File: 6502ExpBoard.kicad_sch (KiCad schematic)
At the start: 40 parts, among them J2 Expansion / Diag Port, U1 74LS373, U2 74LS373, U4 74LS373

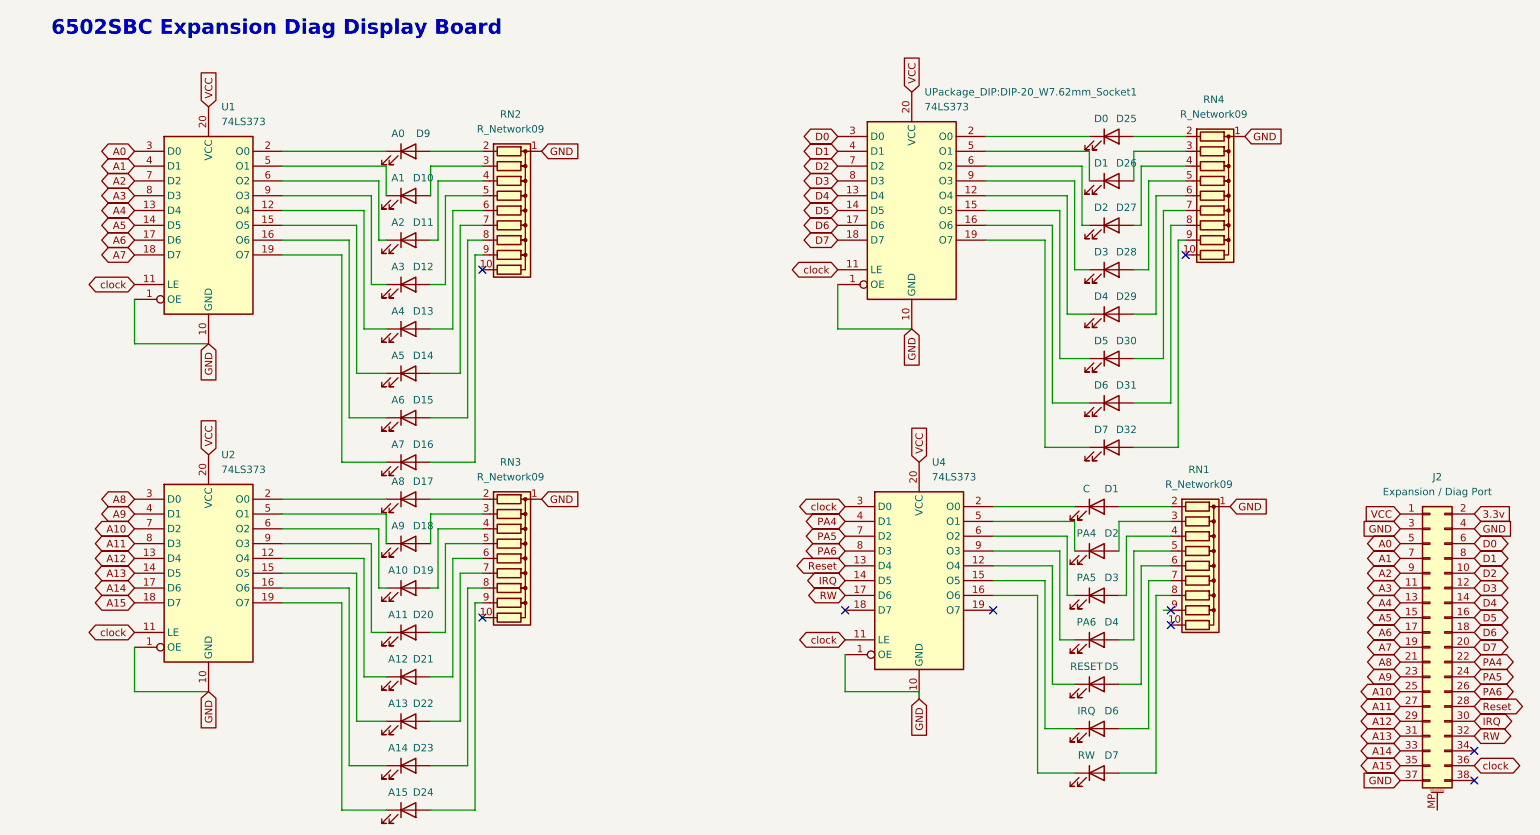
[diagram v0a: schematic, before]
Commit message: Diag Board led fixes
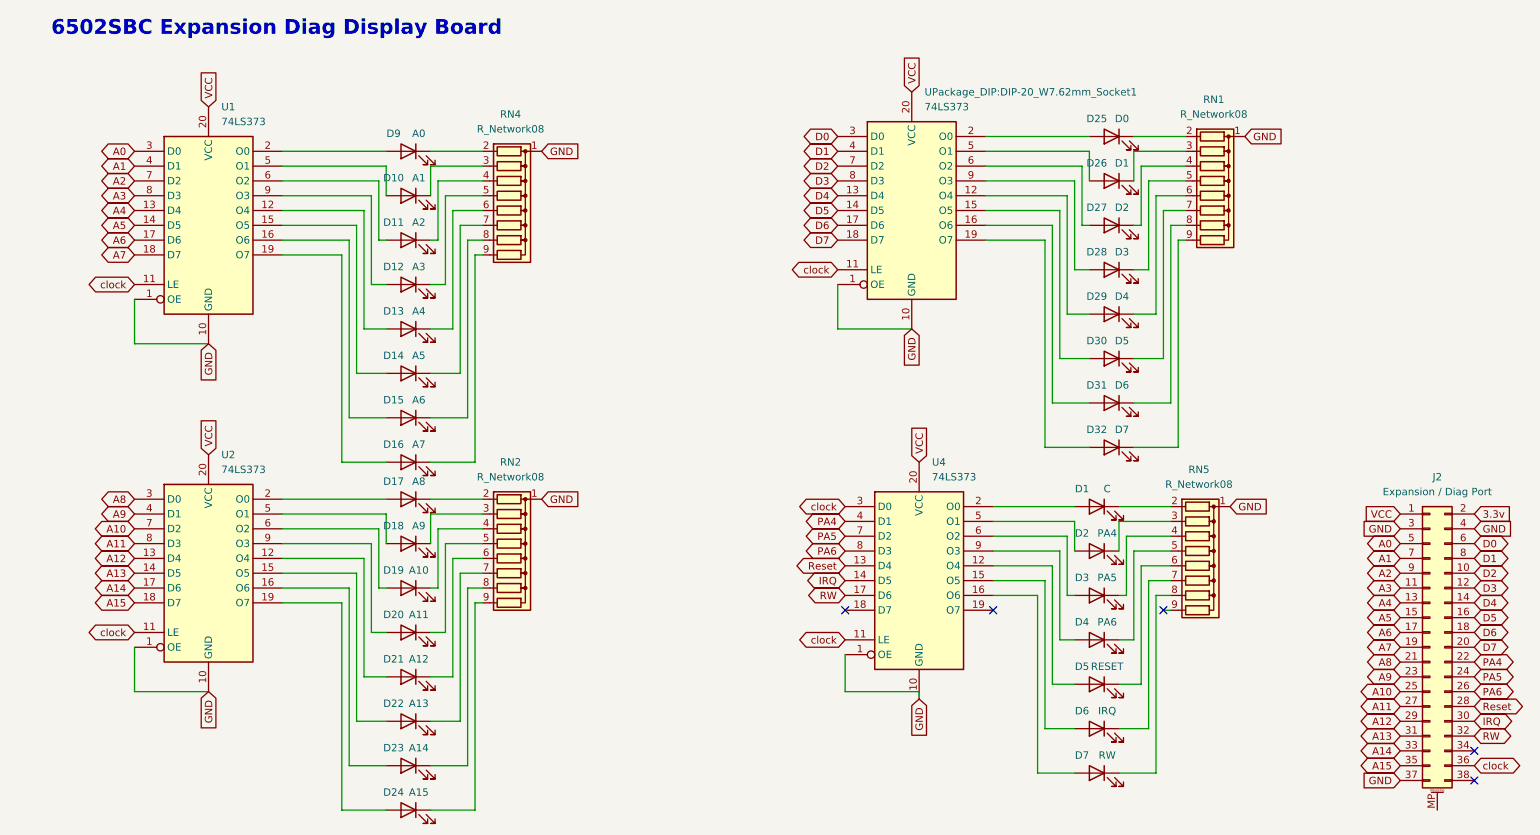
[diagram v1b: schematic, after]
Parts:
- removed RN1, RN2, RN3, RN4: R_Network09, Resistor_THT:R_Array_SIP10, symbol Device:R_Network09
- added RN1, RN2, RN4, RN5: R_Network08, Resistor_THT:R_Array_SIP9, symbol Device:R_Network08
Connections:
- net GND: now also RN1.1 (common), RN2.1 (common), RN4.1 (common), RN5.1 (common)
- net at D18.1 (K): now also RN2.3 (R2); no longer U2.5 (O1)
- net at D18.2 (A): now also U2.5 (O1)
- net at D24.1 (K): now also RN2.9 (R8); no longer U2.19 (O7)
- net at D24.2 (A): now also U2.19 (O7)
- net at D6.1 (K): now also RN5.7 (R6); no longer U4.15 (O5)
- net at D6.2 (A): now also U4.15 (O5)
- net at U4.12 (O4): now also D5.2 (A); no longer D5.1 (K)
- net at U4.16 (O6): now also D7.2 (A); no longer D7.1 (K)
- net at U4.2 (O0): now also D1.2 (A); no longer D1.1 (K)
- net at U4.5 (O1): now also D2.2 (A); no longer D2.1 (K)
- net at U4.6 (O2): now also D3.2 (A); no longer D3.1 (K)
- net at U4.9 (O3): now also D4.2 (A); no longer D4.1 (K)
- net at D17.1 (K): now also RN2.2 (R1); no longer U2.2 (O0)
- net at D17.2 (A): now also U2.2 (O0)
- net at D19.1 (K): now also RN2.4 (R3); no longer U2.6 (O2)
- net at D19.2 (A): now also U2.6 (O2)
- net at D23.1 (K): now also RN2.8 (R7); no longer U2.16 (O6)
- net at D23.2 (A): now also U2.16 (O6)
- net at D27.1 (K): now also RN1.4 (R3); no longer UPackage_DIP:DIP-20_W7.62mm_Socket1.6 (O2)
- net at D27.2 (A): now also UPackage_DIP:DIP-20_W7.62mm_Socket1.6 (O2)
- net at D26.1 (K): now also RN1.3 (R2); no longer UPackage_DIP:DIP-20_W7.62mm_Socket1.5 (O1)
- net at D26.2 (A): now also UPackage_DIP:DIP-20_W7.62mm_Socket1.5 (O1)
- net at D14.1 (K): now also RN4.7 (R6); no longer U1.15 (O5)
- net at D14.2 (A): now also U1.15 (O5)
- net at D30.1 (K): now also RN1.7 (R6); no longer UPackage_DIP:DIP-20_W7.62mm_Socket1.15 (O5)
- net at D30.2 (A): now also UPackage_DIP:DIP-20_W7.62mm_Socket1.15 (O5)
- net at D31.1 (K): now also RN1.8 (R7); no longer UPackage_DIP:DIP-20_W7.62mm_Socket1.16 (O6)
- net at D31.2 (A): now also UPackage_DIP:DIP-20_W7.62mm_Socket1.16 (O6)
- net at D20.2 (A): now also U2.9 (O3)
- net at D21.2 (A): now also U2.12 (O4)
- net at D22.2 (A): now also U2.15 (O5)
- net at D10.1 (K): now also RN4.3 (R2); no longer U1.5 (O1)
- net at D10.2 (A): now also U1.5 (O1)
- net at D11.1 (K): now also RN4.4 (R3); no longer U1.6 (O2)
- net at D11.2 (A): now also U1.6 (O2)
- net at D22.1 (K): now also RN2.7 (R6); no longer U2.15 (O5)
- net at D29.1 (K): now also RN1.6 (R5); no longer UPackage_DIP:DIP-20_W7.62mm_Socket1.12 (O4)
- net at D32.1 (K): now also RN1.9 (R8); no longer UPackage_DIP:DIP-20_W7.62mm_Socket1.19 (O7)
- net at D25.1 (K): now also RN1.2 (R1); no longer UPackage_DIP:DIP-20_W7.62mm_Socket1.2 (O0)
- net at D28.1 (K): now also RN1.5 (R4); no longer UPackage_DIP:DIP-20_W7.62mm_Socket1.9 (O3)
- net at D25.2 (A): now also UPackage_DIP:DIP-20_W7.62mm_Socket1.2 (O0)
- net at D28.2 (A): now also UPackage_DIP:DIP-20_W7.62mm_Socket1.9 (O3)
- net at D29.2 (A): now also UPackage_DIP:DIP-20_W7.62mm_Socket1.12 (O4)
- net at D32.2 (A): now also UPackage_DIP:DIP-20_W7.62mm_Socket1.19 (O7)
- net at D15.1 (K): now also RN4.8 (R7); no longer U1.16 (O6)
- net at D15.2 (A): now also U1.16 (O6)
- net at D13.1 (K): now also RN4.6 (R5); no longer U1.12 (O4)
- net at D16.1 (K): now also RN4.9 (R8); no longer U1.19 (O7)
- net at D9.1 (K): now also RN4.2 (R1); no longer U1.2 (O0)
- net at D12.1 (K): now also RN4.5 (R4); no longer U1.9 (O3)
- net at D16.2 (A): now also U1.19 (O7)
- net at D20.1 (K): now also RN2.5 (R4); no longer U2.9 (O3)
- net at D21.1 (K): now also RN2.6 (R5); no longer U2.12 (O4)
- net at D13.2 (A): now also U1.12 (O4)
- net at D9.2 (A): now also U1.2 (O0)
- net at D12.2 (A): now also U1.9 (O3)
- new net: D5.1 (K), RN5.6 (R5)
- new net: D1.1 (K), RN5.2 (R1)
- new net: D2.1 (K), RN5.3 (R2)
- new net: D7.1 (K), RN5.8 (R7)
- new net: D4.1 (K), RN5.5 (R4)
- new net: D3.1 (K), RN5.4 (R3)
- no-connect marks 9 -> 5
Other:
- moved on the sheet: D1, D10, D11, D12, D13, D14, D15, D16, D17, D18, D19, D2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
